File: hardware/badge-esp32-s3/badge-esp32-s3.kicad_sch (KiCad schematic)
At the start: 4 parts, among them U1 ESP32-S3-MINI-1-N8

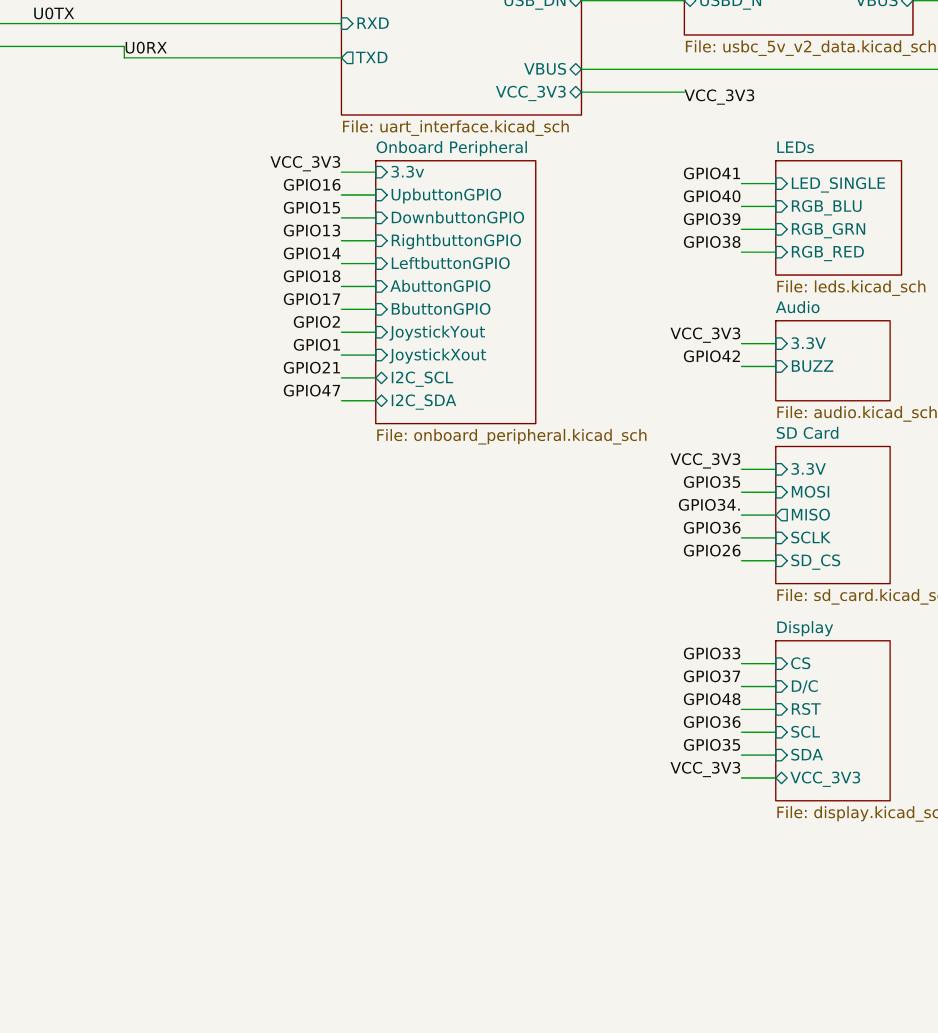
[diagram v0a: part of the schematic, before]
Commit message: Updated the PCB to have the gpio jumper pins.
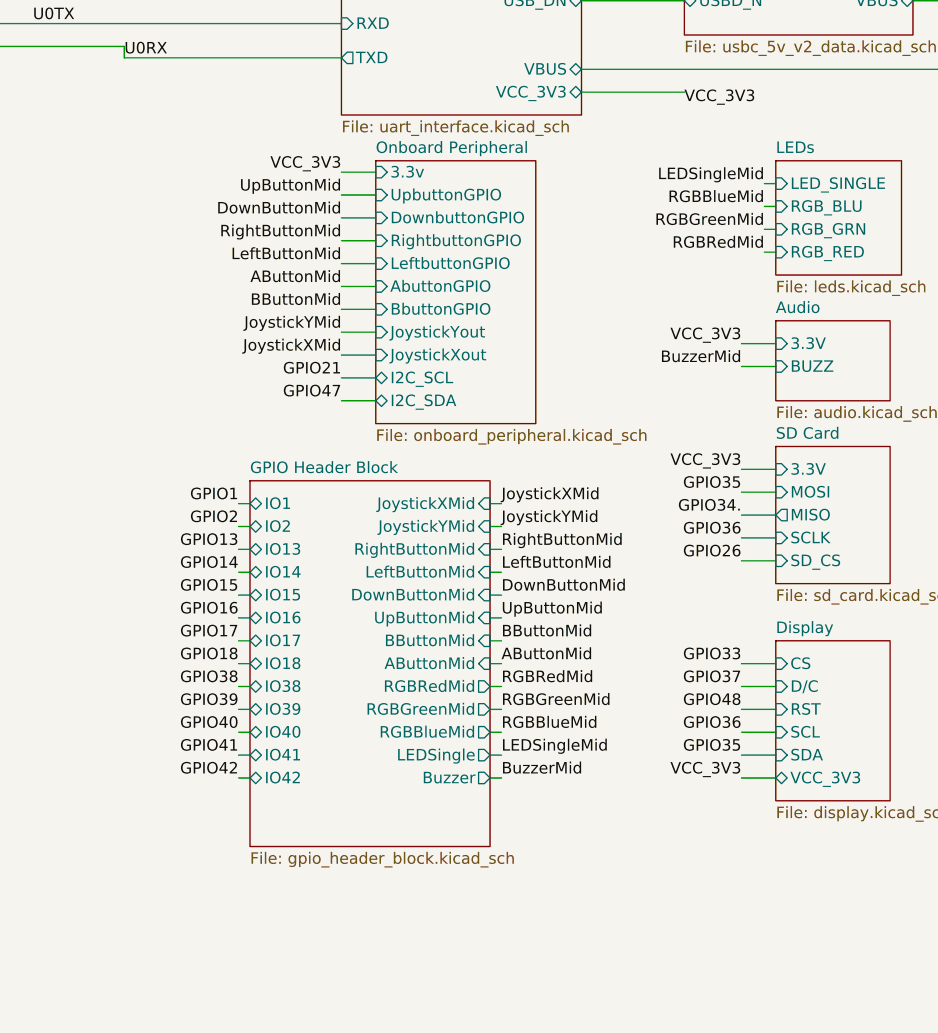
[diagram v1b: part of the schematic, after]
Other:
- added sheet GPIO Header Block (gpio_header_block.kicad_sch)

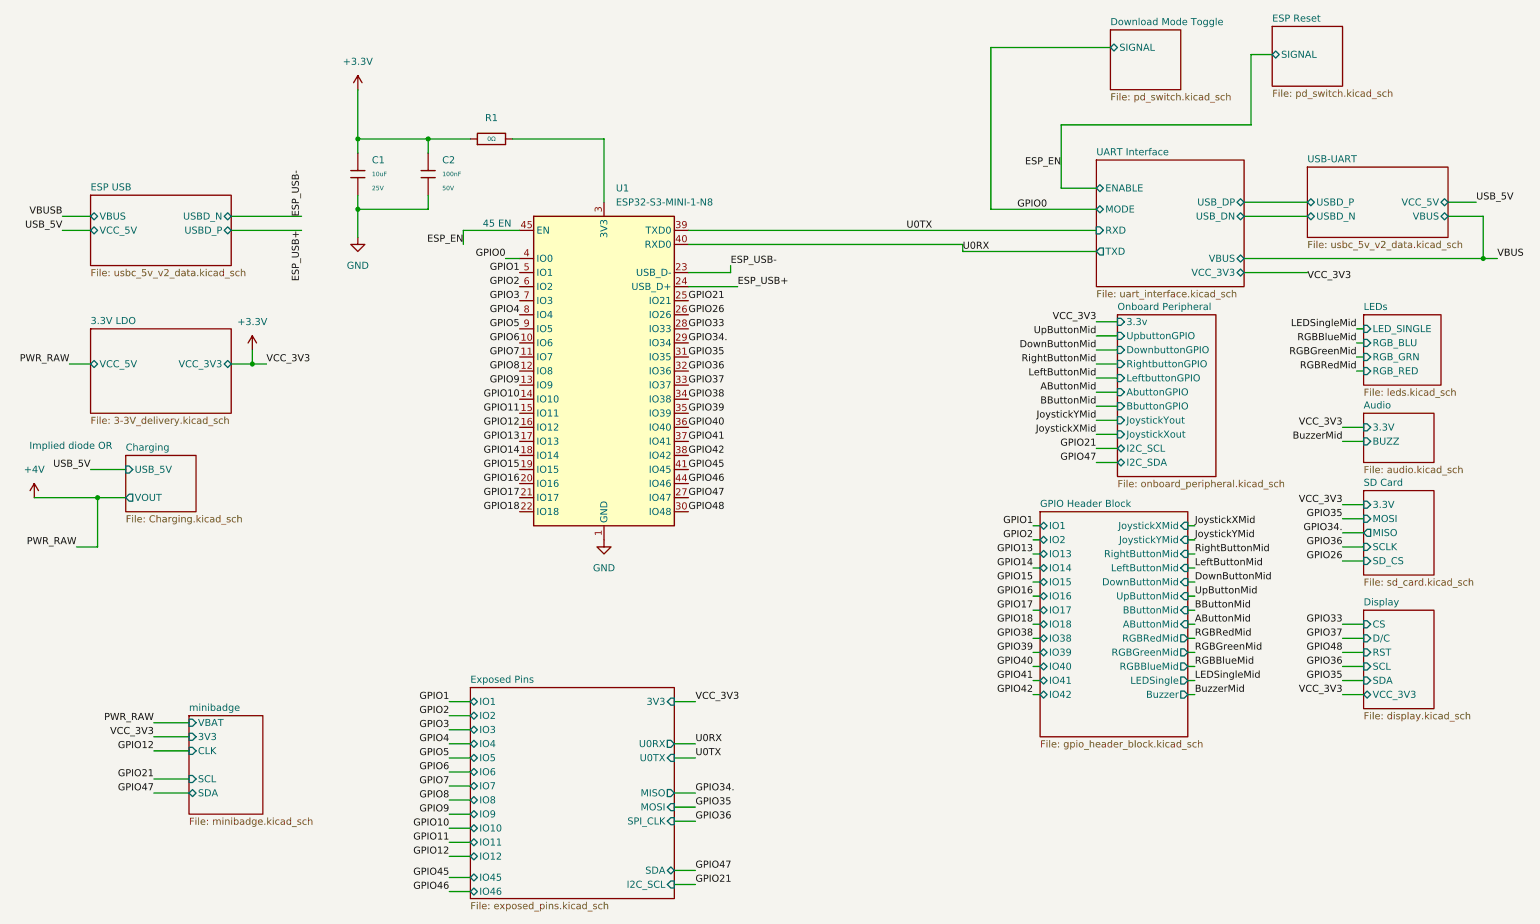
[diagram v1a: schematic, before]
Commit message: Consolidated the GPIO pins, communication pins, and power pins.
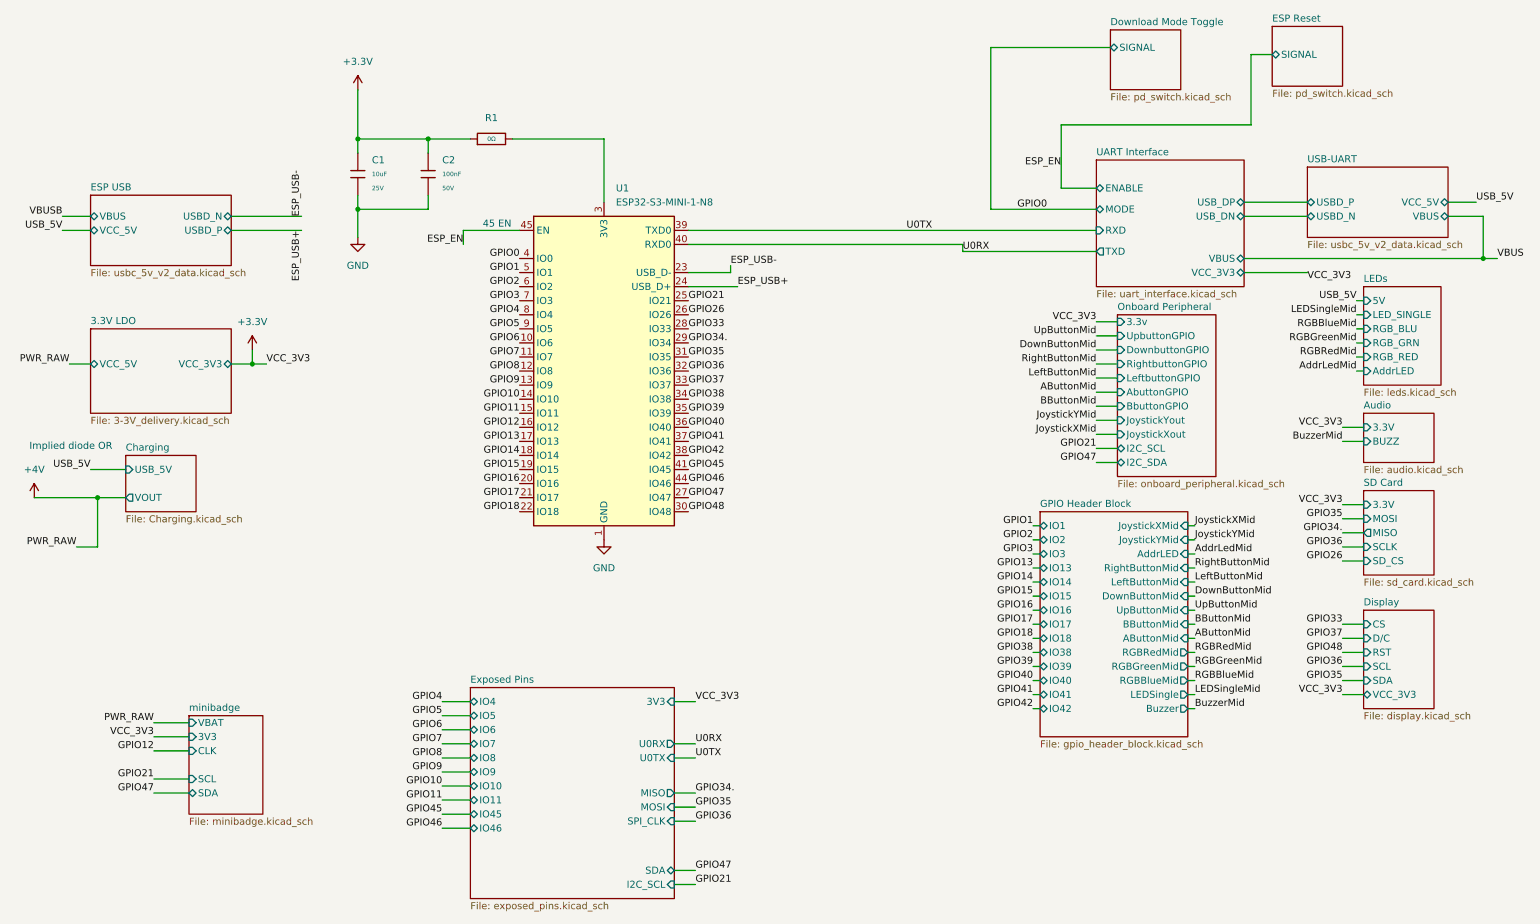
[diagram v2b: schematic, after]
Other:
- sheet Exposed Pins ports: added none; removed IO1, IO12, IO2, IO3
- sheet GPIO Header Block ports: added AddrLED, IO3; removed none
- sheet LEDs ports: added 5V, AddrLED; removed none

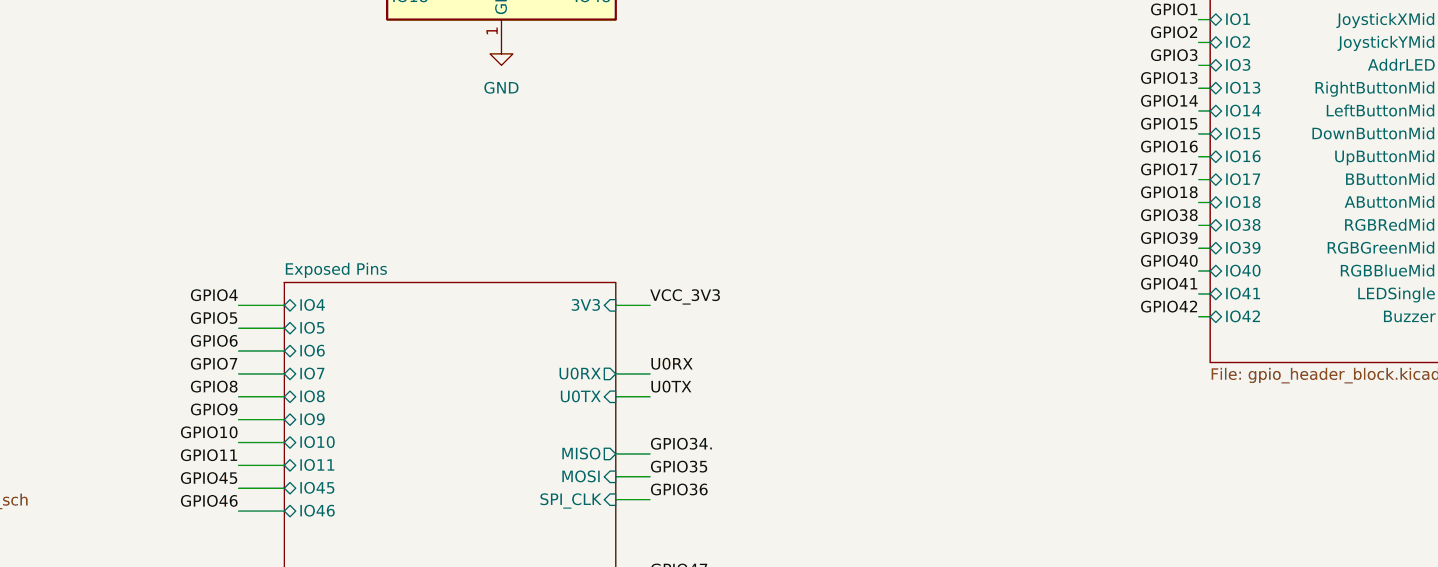
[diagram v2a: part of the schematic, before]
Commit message: Swapped the RGB led pins.
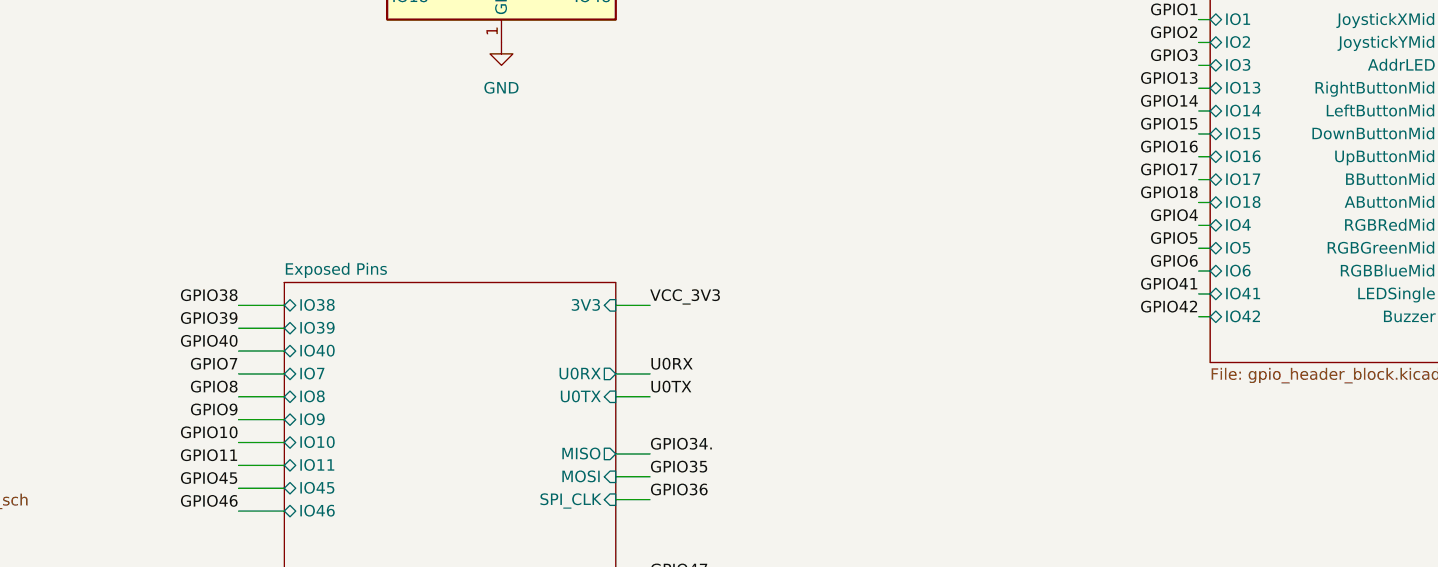
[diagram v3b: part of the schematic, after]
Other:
- sheet Exposed Pins ports: added IO38, IO39, IO40; removed IO4, IO5, IO6
- sheet GPIO Header Block ports: added IO4, IO5, IO6; removed IO38, IO39, IO40
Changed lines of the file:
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@@
 		)
 	)
-	(label "GPIO38"
+	(label "GPIO4"
 		(at 195.58 128.27 180)
 		(effects
@@
 		)
 	)
-	(label "GPIO4"
+	(label "GPIO38"
 		(at 88.9 137.16 180)
 		(effects
@@
 		)
 	)
-	(label "GPIO40"
+	(label "GPIO6"
 		(at 195.58 133.35 180)
 		(effects
@@
 		)
 	)
-	(label "GPIO5"
+	(label "GPIO39"
 		(at 88.9 139.7 180)
 		(effects
@@
 		)
 	)
-	(label "GPIO39"
+	(label "GPIO5"
 		(at 195.58 130.81 180)
 		(effects
@@
 		)
 	)
-	(label "GPIO6"
+	(label "GPIO40"
 		(at 88.9 142.24 180)
 		(effects
@@
 			)
 		)
-		(pin "IO4" bidirectional
+		(pin "IO38" bidirectional
 			(at 93.98 137.16 180)
 			(effects
@@
 			)
 		)
-		(pin "IO5" bidirectional
+		(pin "IO39" bidirectional
 			(at 93.98 139.7 180)
 			(effects
@@
 			)
 		)
-		(pin "IO6" bidirectional
+		(pin "IO40" bidirectional
 			(at 93.98 142.24 180)
 			(effects
@@
 			)
 		)
-		(pin "IO38" bidirectional
+		(pin "IO4" bidirectional
 			(at 196.85 128.27 180)
 			(effects
@@
 			)
 		)
-		(pin "IO39" bidirectional
+		(pin "IO5" bidirectional
 			(at 196.85 130.81 180)
 			(effects
@@
 			)
 		)
-		(pin "IO40" bidirectional
+		(pin "IO6" bidirectional
 			(at 196.85 133.35 180)
 			(effects

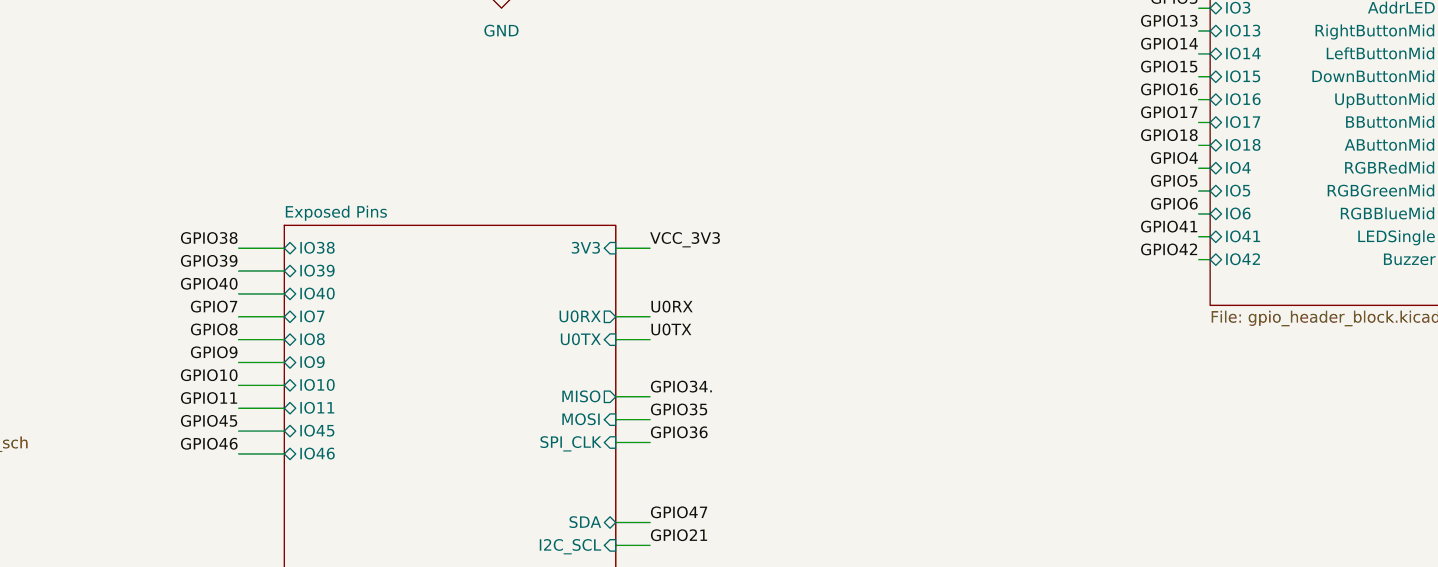
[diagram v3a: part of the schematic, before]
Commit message: Updated the buzzer to not use a jtag pin.
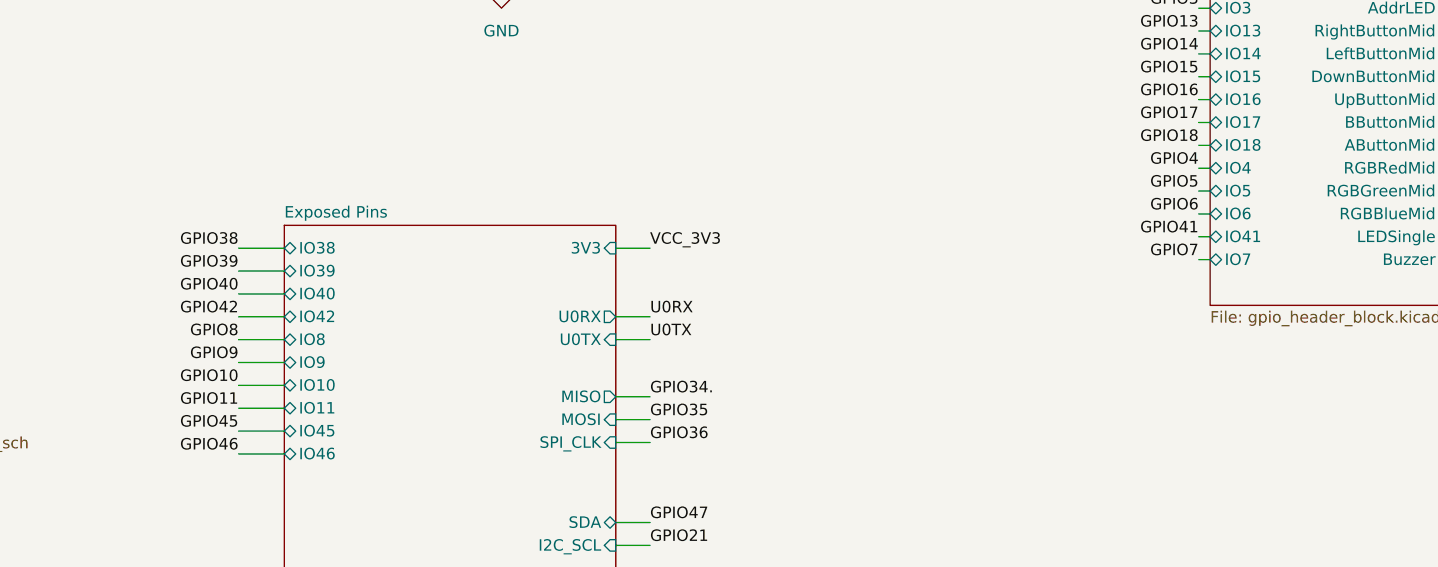
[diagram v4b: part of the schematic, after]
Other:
- sheet Exposed Pins ports: added IO42; removed IO7
- sheet GPIO Header Block ports: added IO7; removed IO42
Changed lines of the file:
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@@
 		)
 	)
-	(label "GPIO42"
+	(label "GPIO7"
 		(at 195.58 138.43 180)
 		(effects
@@
 		)
 	)
-	(label "GPIO7"
+	(label "GPIO42"
 		(at 88.9 144.78 180)
 		(effects
@@
 			)
 		)
-		(pin "IO7" bidirectional
+		(pin "IO42" bidirectional
 			(at 93.98 144.78 180)
 			(effects
@@
 			)
 		)
-		(pin "IO42" bidirectional
+		(pin "IO7" bidirectional
 			(at 196.85 138.43 180)
 			(effects
